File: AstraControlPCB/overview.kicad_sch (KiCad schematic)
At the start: 0 parts

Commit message: Update wks file
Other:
- company: (none) -> LiveAstra Technologies
- title: Overview -> AstraControl - Root
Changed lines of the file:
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@@
 	(paper "A4")
 	(title_block
-		(title "Overview")
+		(title "AstraControl - Root")
+		(date "2024-08-26")
+		(rev "A")
+		(company "LiveAstra Technologies")
 	)
 	(polyline
@@
 		(effects
 			(font
-				(face "Sarabun")
+				(face "ING Me")
 				(size 3 3)
 				(color 255 255 255 1)
@@
 		(effects
 			(font
-				(face "Sarabun")
+				(face "ING Me")
 				(size 3 3)
 				(color 255 255 255 1)
@@
 		(effects
 			(font
-				(face "Sarabun")
+				(face "ING Me")
 				(size 3 3)
 				(color 255 255 255 1)
@@
 		(effects
 			(font
-				(face "Sarabun")
+				(face "ING Me")
 				(size 3 3)
 				(color 255 255 255 1)
@@
 		(effects
 			(font
-				(face "Sarabun")
+				(face "ING Me")
 				(size 3 3)
 				(color 255 255 255 1)
@@
 		(effects
 			(font
-				(face "Sarabun ExtraBold")
+				(face "ING Me")
 				(size 4 4)
 				(color 255 255 255 1)
@@
 		(effects
 			(font
-				(face "Sarabun ExtraBold")
+				(face "ING Me")
 				(size 4 4)
 				(color 255 255 255 1)
@@
 		(effects
 			(font
-				(face "Sarabun")
+				(face "ING Me")
 				(size 3 3)
 				(color 255 255 255 1)
@@
 		(effects
 			(font
-				(face "Sarabun ExtraBold")
+				(face "ING Me")
 				(size 5 5)
 				(color 255 255 255 1)
@@
 		(effects
 			(font
-				(face "Sarabun")
+				(face "ING Me")
 				(size 3 3)
 				(color 255 255 255 1)
@@
 		(effects
 			(font
-				(face "Sarabun ExtraBold")
+				(face "ING Me")
 				(size 4 4)
 				(color 255 255 255 1)
@@
 		(effects
 			(font
-				(face "Sarabun")
+				(face "ING Me")
 				(size 1.5 1.5)
 				(color 255 255 255 1)
@@
 		(effects
 			(font
-				(face "Sarabun ExtraBold")
+				(face "ING Me")
 				(size 4 4)
 				(color 255 255 255 1)
@@
 		(effects
 			(font
-				(face "Sarabun")
+				(face "ING Me")
 				(size 1.5 1.5)
 				(color 255 255 255 1)
@@
 		(effects
 			(font
-				(face "Sarabun")
+				(face "ING Me")
 				(size 1.5 1.5)
 				(color 255 255 255 1)
@@
 		(effects
 			(font
-				(face "Sarabun")
+				(face "ING Me")
 				(size 8 8)
 				(color 255 255 255 1)
@@
 		(effects
 			(font
-				(face "Sarabun")
+				(face "ING Me")
 				(size 3 3)
 				(color 255 255 255 1)
@@
 		(effects
 			(font
-				(face "Sarabun")
+				(face "ING Me")
 				(size 3 3)
 				(color 255 255 255 1)
@@
 		(effects
 			(font
-				(face "Sarabun")
+				(face "ING Me")
 				(size 3 3)
 				(color 255 255 255 1)
@@
 		(effects
 			(font
-				(face "Sarabun ExtraBold")
+				(face "ING Me")
 				(size 4 4)
 				(color 255 255 255 1)
@@
 		(effects
 			(font
-				(face "Sarabun")
+				(face "ING Me")
 				(size 3 3)
 				(color 255 255 255 1)
@@
 		(effects
 			(font
-				(face "Sarabun ExtraBold")
+				(face "ING Me")
 				(size 4 4)
 				(color 255 255 255 1)
@@
 		(effects
 			(font
-				(face "Sarabun")
+				(face "ING Me")
 				(size 3 3)
 				(color 255 255 255 1)
@@
 		(effects
 			(font
-				(face "Sarabun")
+				(face "ING Me")
 				(size 3 3)
 				(color 255 255 255 1)
@@
 		(effects
 			(font
-				(face "Sarabun")
+				(face "ING Me")
 				(size 3 3)
 				(color 255 255 255 1)
@@
 		(effects
 			(font
-				(face "Sarabun")
+				(face "ING Me")
 				(size 3 3)
 				(color 255 255 255 1)
@@
 		(effects
 			(font
-				(face "Sarabun")
+				(face "ING Me")
 				(size 3 3)
 				(color 255 255 255 1)
@@
 		(effects
 			(font
-				(face "Sarabun")
+				(face "ING Me")
 				(size 3 3)
 				(color 255 255 255 1)
@@
 		(effects
 			(font
-				(face "Sarabun ExtraBold")
+				(face "ING Me")
 				(size 4 4)
 				(color 255 255 255 1)
@@
 		(effects
 			(font
-				(face "Sarabun")
-				(size 3 3)
-				(color 255 255 255 1)
+				(face "ING Me")
+				(size 3 3)
+				(color 255 255 255 1)

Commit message: workflow
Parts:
- added I2: ~, symbol LiveAstra:Information_Box
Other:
- note added: "MCU Enable and Boot"
- note added: "Second time creating a PCB. Mistakes were probably made."
- note added: "Some features are not necessary but used as a learning experience and experimentation."
- note removed: "Components marked with will not be fitted."
- note removed: "MCU Power"
- note removed: "Render placeholder"

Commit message: workflow
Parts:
- removed I2: ~, symbol LiveAstra:Information_Box
- added CRT2: ~, symbol LiveAstra:Critical_Box
- added INF1: ~, symbol LiveAstra:Information_Box
- added QST1: ~, symbol LiveAstra:Question_Box
- added WRN1: ~, symbol LiveAstra:Warning_Box
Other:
- note removed: "Caution"
- note removed: "Critical"
- note removed: "Design Considerations"
- note removed: "Extra care is required here. Pay attention to details, routing, and try your best to follow the advice."
- note removed: "Generic information box to inform about specifics of the part or layout, notes, helpful information."
- note removed: "Information"
- note removed: "It is critical to follow the instructions here. Failure to do so will result in poor performance or failuire."

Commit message: update
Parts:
- renumbered CRT2 to CRT1
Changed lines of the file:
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@@
 		(dnp no)
 		(fields_autoplaced yes)
-		(property "Reference" "CRT2"
+		(property "Reference" "CRT1"
 			(at 158.75 147.32 0)
 			(effects
@@
 			(project ""
 				(path "/9a751838-dce8-4d69-8a02-736625ac74e7/120c81b5-e37e-42ba-9ea8-918058b1f430"
-					(reference "CRT2")
+					(reference "CRT1")
 					(unit 1)
 				)

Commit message: update
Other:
- note added: "10"
- note added: "11"
- note added: "12"
- note added: "13"
- note added: "14"
- note added: "15"
- note added: "16"
- note added: "3.3V to 5V Logic Shifter"
- note added: "5V GPIO Connectors"
- note added: "5V Protection"
- note added: "8"
- note added: "9"
- note added: "Button, Status LED, UART, I2S"
- note added: "Extra care is required here. Pay attention to details, routing, and try your best to follow the advice."
- note added: "Fan, Temperature, Screen I2C"
- note added: "Generic information box to inform about specifics of the part or layout, notes, helpful information."
- note added: "It is critical to follow the instructions here. Failure to do so will result in poor performance or failuire."
- note added: "PWM Connector"
- note added: "Something is unclear or a missing piece of information potentially needs to be explored further."
- note added: "UART to RS-485"
- note added: "USB-C"
- note removed: "LED Drivers"

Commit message: Updates
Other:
- note added: "PCB components are spread apart a bit more than the minimum allowed clearance for easy debuging and adjustments."
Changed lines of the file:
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@@
+	)
+	(circle
+		(center 22.86 134.62)
+		(radius 0.6351)
+		(stroke
+			(width -0.0001)
+			(type default)
+		)
+		(fill
+			(type color)
+			(color 0 0 0 0)
+		)
 	)
 	(circle
@@
 		(effects
 			(font
+				(face "ING Me")
+				(size 3 3)
+			)
+			(justify left)
+		)
+	)
+	(text "PCB components are spread apart a bit more than the minimum allowed clearance for easy debuging and adjustments."
+		(exclude_from_sim no)
+		(at 25.4 135.89 0)
+		(effects
+			(font

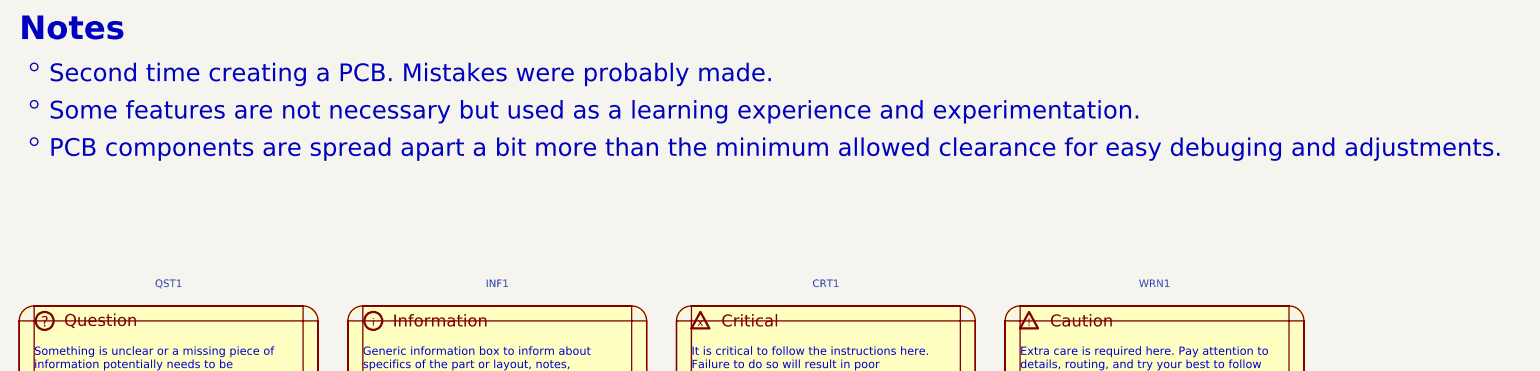
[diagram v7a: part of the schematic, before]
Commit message: RS485 tranceiver changed and TVS
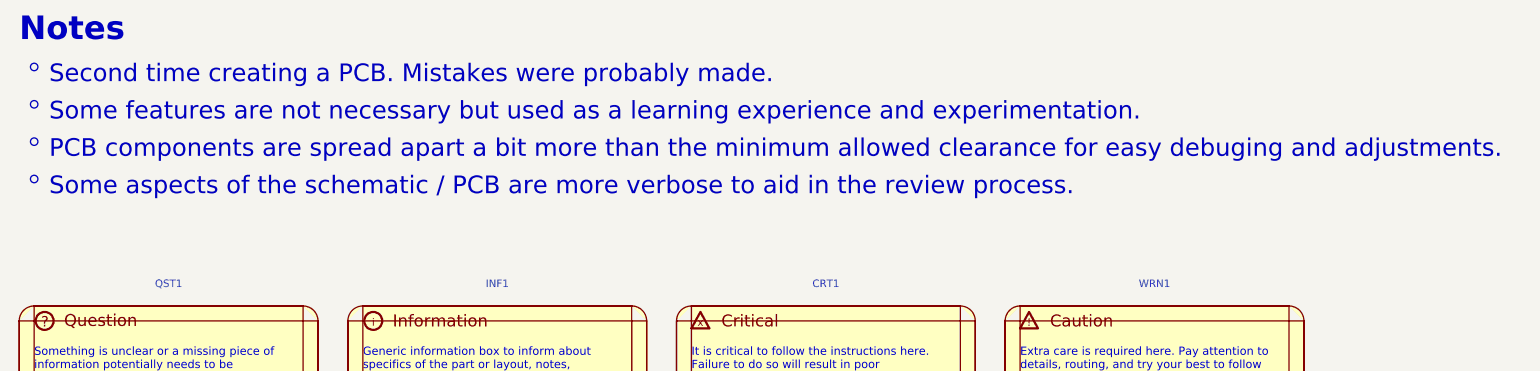
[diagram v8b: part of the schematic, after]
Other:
- note added: "Some aspects of the schematic / PCB are more verbose to aid in the review process."
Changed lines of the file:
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@@
+	)
+	(circle
+		(center 22.86 140.97)
+		(radius 0.6351)
+		(stroke
+			(width -0.0001)
+			(type default)
+		)
+		(fill
+			(type color)
+			(color 0 0 0 0)
+		)
 	)
 	(circle
@@
 			)
 			(justify left)
+		)
+	)
+	(text "Some aspects of the schematic / PCB are more verbose to aid in the review process."
+		(exclude_from_sim no)
+		(at 25.4 142.24 0)
+		(effects
+			(font
+				(face "ING Me")
+				(size 3 3)
+			)
+			(justify left)
